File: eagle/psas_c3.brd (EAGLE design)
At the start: 100 x 80 mm, 61 parts, among them IC1 CP2102, U1 MIC5219 3.3V, Y1 32MHz

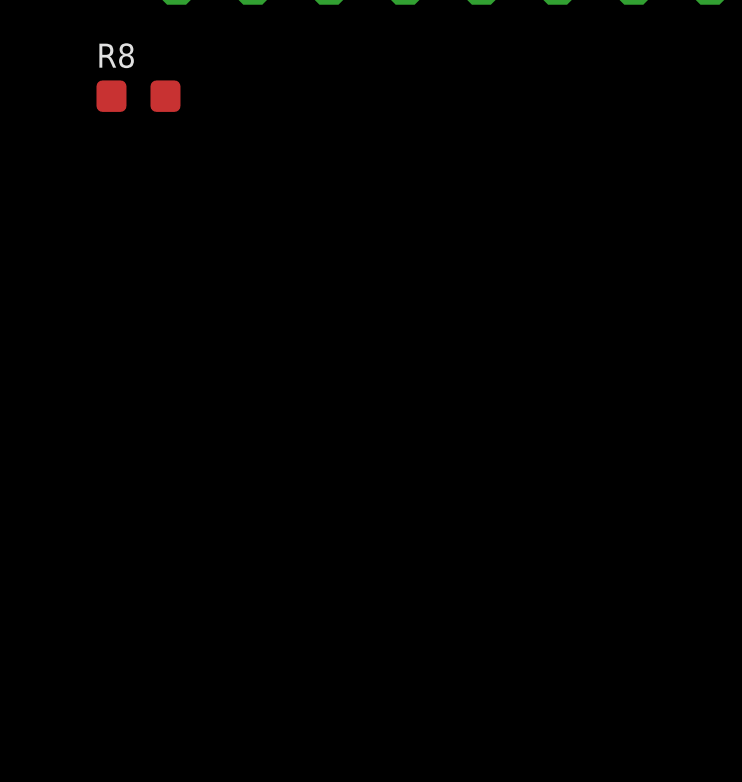
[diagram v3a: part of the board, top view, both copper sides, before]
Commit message: Added GPIO 2x9pins, 2x10 pins and SW Connector
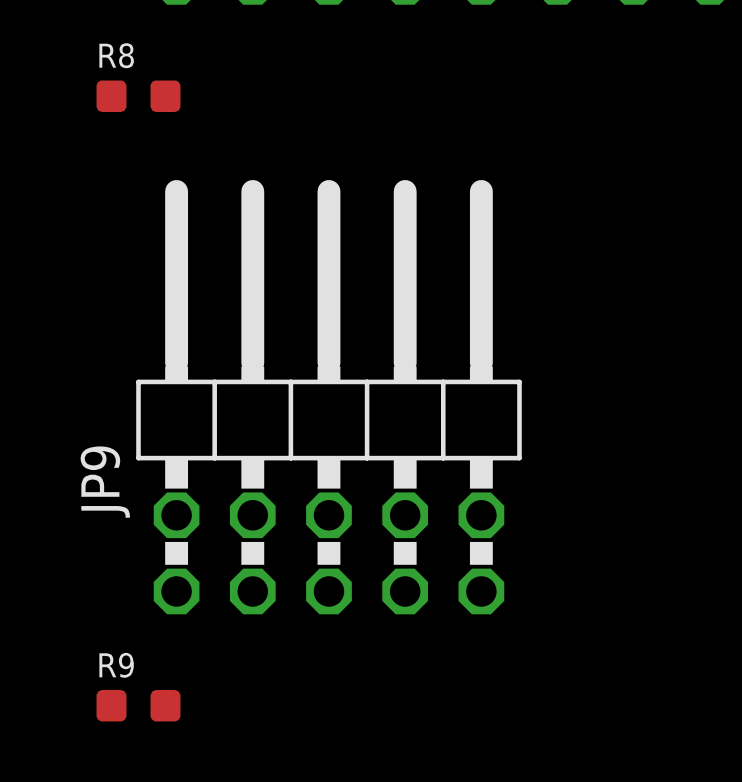
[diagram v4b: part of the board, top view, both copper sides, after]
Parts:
- added JP9: (no value), pinhead:2X05/90
- added R9: 10k, rcl_custom:.0603-A-NOSILK
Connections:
- new net PTA0: JP9.4, U$1.10
- new net PTA3: JP9.2, R9.1, U$1.11
- net 3.3V: now also R9.2
- net GND: now also JP9.3, JP9.5
- net PTA20: now also JP9.10
- net V+: now also JP9.1
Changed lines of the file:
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@@
 <element name="JP8" library="pinhead" package="2X10/90" value="" x="-63.5" y="-107.95"/>
 <element name="R8" library="rcl_custom" package=".0603-A-NOSILK" value="0" x="-76.2" y="-118.11"/>
+<element name="JP9" library="pinhead" package="2X05/90" value="" x="-69.85" y="-128.27"/>
+<element name="R9" library="rcl_custom" package=".0603-A-NOSILK" value="10k" x="-76.2" y="-138.43"/>
 </elements>
 <signals>
@@
 <contactref element="JP8" pad="15"/>
 <contactref element="JP8" pad="3"/>
+<contactref element="JP9" pad="5"/>
+<contactref element="JP9" pad="3"/>
+<wire x1="-69.85" y1="-134.62" x2="-72.39" y2="-134.62" width="0" layer="19" extent="1-1"/>
+<wire x1="-72.39" y1="-114.3" x2="-72.39" y2="-134.62" width="0" layer="19" extent="1-1"/>
 <wire x1="-57.15" y1="-114.3" x2="-72.39" y2="-114.3" width="0" layer="19" extent="1-1"/>
 <wire x1="-62.23" y1="-86.36" x2="-57.15" y2="-114.3" width="0" layer="19" extent="1-1"/>
@@
 <contactref element="R6" pad="2"/>
 <contactref element="JP5" pad="1"/>
+<contactref element="R9" pad="2"/>
+<wire x1="-66.51" y1="-73.66" x2="-75.3" y2="-138.43" width="0" layer="19" extent="1-1"/>
 <wire x1="-67.31" y1="-58.42" x2="-66.51" y2="-73.66" width="0" layer="19" extent="1-1"/>
 <wire x1="-56.68" y1="-44.45" x2="-67.31" y2="-58.42" width="0" layer="19" extent="1-1"/>
@@
 </signal>
 <signal name="VBUS">
-<contactref element="U2" pad="P$18"/>
-<contactref element="U2" pad="P$2"/>
-<contactref element="U2" pad="P$19"/>
-<contactref element="C1" pad="1"/>
-<contactref element="U2" pad="P$9"/>
-<contactref element="U2" pad="P$3"/>
 <contactref element="C17" pad="1"/>
 <contactref element="CF1" pad="1"/>
@@
 <contactref element="IC1" pad="7"/>
 <contactref element="LED1" pad="2"/>
+<contactref element="U2" pad="P$19"/>
+<contactref element="U2" pad="P$3"/>
+<contactref element="U2" pad="P$9"/>
+<contactref element="U2" pad="P$2"/>
+<contactref element="U2" pad="P$18"/>
+<contactref element="C1" pad="1"/>
 <contactref element="TP5" pad="1"/>
 <wire x1="-56.68" y1="-58.97" x2="-60.96" y2="-66.04" width="0" layer="19" extent="1-1"/>
@@
 <contactref element="JP6" pad="1"/>
 <contactref element="JP8" pad="1"/>
+<contactref element="JP9" pad="1"/>
+<wire x1="-74.93" y1="-114.3" x2="-74.93" y2="-134.62" width="0" layer="19" extent="1-1"/>
 <wire x1="-64.77" y1="-88.9" x2="-74.93" y2="-114.3" width="0" layer="19" extent="1-1"/>
 <wire x1="-39.1" y1="4.35" x2="-64.77" y2="-88.9" width="0" layer="19" extent="1-1"/>
@@
 <contactref element="S2" pad="A2"/>
 <contactref element="JP8" pad="10"/>
+<contactref element="JP9" pad="10"/>
+<wire x1="-64.77" y1="-111.76" x2="-64.77" y2="-132.08" width="0" layer="19" extent="1-1"/>
 <wire x1="-20.405" y1="24.11" x2="-64.77" y2="-111.76" width="0" layer="19" extent="1-1"/>
 <wire x1="-18.885" y1="28.23" x2="-20.405" y2="24.11" width="0" layer="19" extent="1-1"/>
@@
 <wire x1="-35.56" y1="29.21" x2="-26.38" y2="19.135" width="0" layer="19" extent="1-1"/>
 </signal>
+<signal name="PTA0">
+<contactref element="U$1" pad="10"/>
+<contactref element="JP9" pad="4"/>
+<wire x1="-27.855" y1="24.11" x2="-72.39" y2="-132.08" width="0" layer="19" extent="1-1"/>
+</signal>
+<signal name="PTA3">
+<contactref element="U$1" pad="11"/>
+<contactref element="JP9" pad="2"/>
+<contactref element="R9" pad="1"/>
+<wire x1="-74.93" y1="-132.08" x2="-77.1" y2="-138.43" width="0" layer="19" extent="1-1"/>
+<wire x1="-27.855" y1="24.61" x2="-74.93" y2="-132.08" width="0" layer="19" extent="1-1"/>
+</signal>
 </signals>

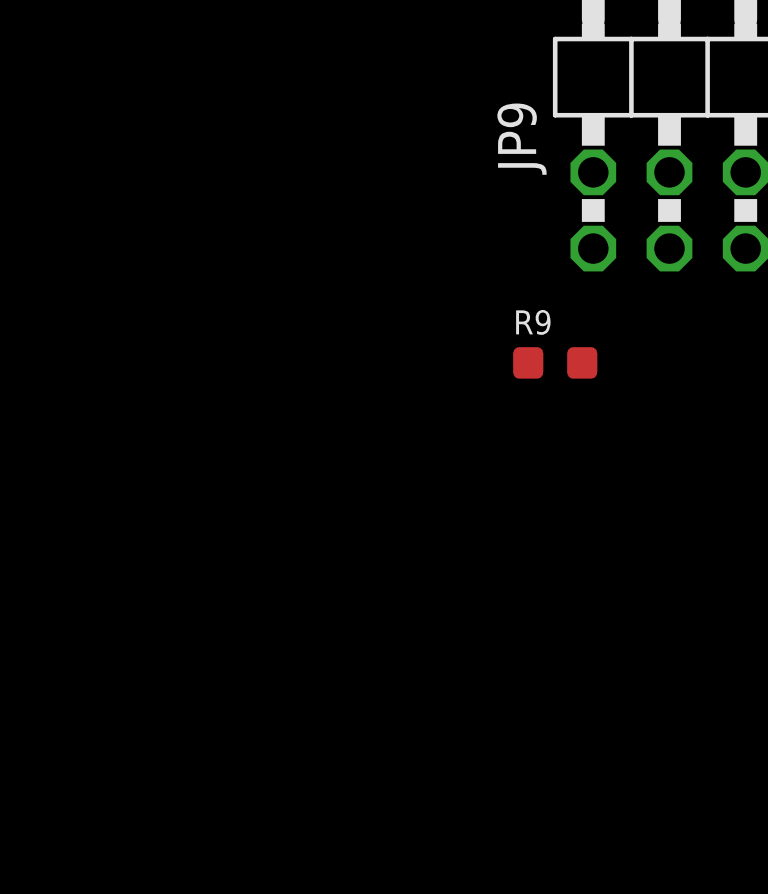
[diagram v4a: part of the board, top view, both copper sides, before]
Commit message: Added Software Development Connector and 32KHz crystal in schematics
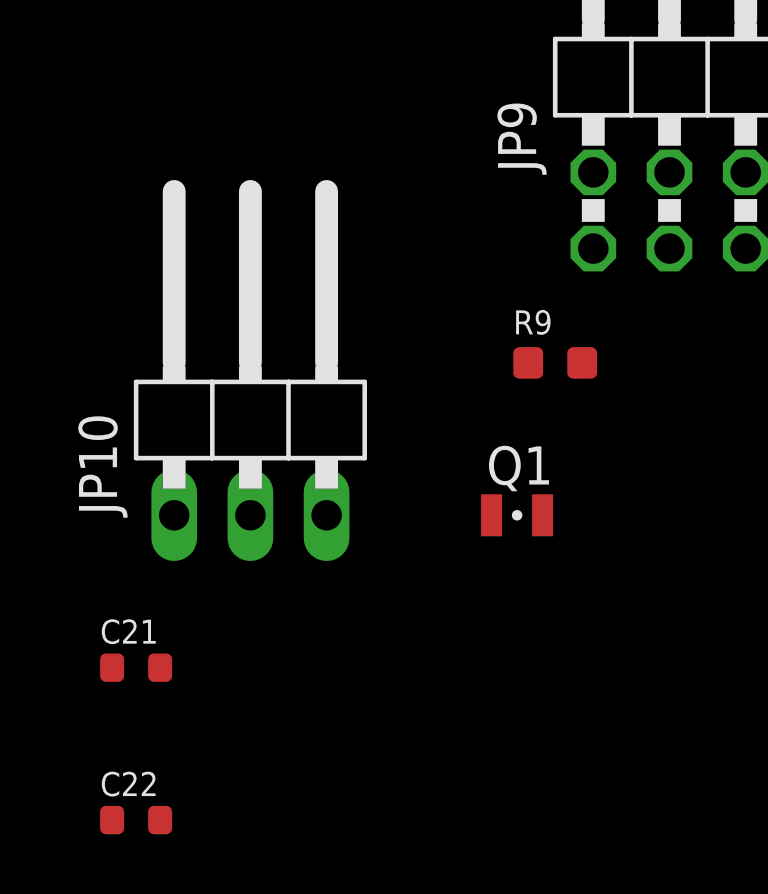
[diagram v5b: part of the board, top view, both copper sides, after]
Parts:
- added C21, C22: 12PF, rcl_custom:.0603-B-NOSILK
- added JP10: (no value), pinhead:1X03/90
- added Q1: FC-12M, crystal:FC-12M
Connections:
- new net N$13: C21.1, JP10.3, Q1.1
- net DIO5: now also JP10.1
- net GND: now also C21.2, C22.2
- net PTA18: now also JP10.2
- net PTA19: now also C22.1, Q1.2
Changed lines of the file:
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@@
 <element name="JP9" library="pinhead" package="2X05/90" value="" x="-69.85" y="-128.27"/>
 <element name="R9" library="rcl_custom" package=".0603-A-NOSILK" value="10k" x="-76.2" y="-138.43"/>
+<element name="Q1" library="crystal" package="FC-12M" value="FC-12M" x="-77.47" y="-143.51"/>
+<element name="JP10" library="pinhead" package="1X03/90" value="" x="-86.36" y="-139.7"/>
+<element name="C21" library="rcl_custom" package=".0603-B-NOSILK" value="12PF" x="-90.17" y="-148.59"/>
+<element name="C22" library="rcl_custom" package=".0603-B-NOSILK" value="12PF" x="-90.17" y="-153.67"/>
 </elements>
 <signals>
@@
 <contactref element="JP9" pad="5"/>
 <contactref element="JP9" pad="3"/>
+<contactref element="C21" pad="2"/>
+<contactref element="C22" pad="2"/>
+<wire x1="-89.37" y1="-148.59" x2="-89.37" y2="-153.67" width="0" layer="19" extent="1-1"/>
+<wire x1="-72.39" y1="-134.62" x2="-89.37" y2="-148.59" width="0" layer="19" extent="1-1"/>
 <wire x1="-69.85" y1="-134.62" x2="-72.39" y2="-134.62" width="0" layer="19" extent="1-1"/>
 <wire x1="-72.39" y1="-114.3" x2="-72.39" y2="-134.62" width="0" layer="19" extent="1-1"/>
@@
 <contactref element="U$1" pad="15"/>
 <contactref element="R8" pad="2"/>
+<contactref element="JP10" pad="2"/>
+<wire x1="-75.3" y1="-118.11" x2="-86.36" y2="-143.51" width="0" layer="19" extent="1-1"/>
 <wire x1="-38.1" y1="29.21" x2="-75.3" y2="-118.11" width="0" layer="19" extent="1-1"/>
 <wire x1="-27.38" y1="26.585" x2="-38.1" y2="29.21" width="0" layer="19" extent="1-1"/>
@@
 <contactref element="U$1" pad="16"/>
 <contactref element="R7" pad="1"/>
+<contactref element="Q1" pad="2"/>
+<contactref element="C22" pad="1"/>
+<wire x1="-76.62" y1="-143.51" x2="-90.97" y2="-153.67" width="0" layer="19" extent="1-1"/>
+<wire x1="-72.02" y1="-97.79" x2="-76.62" y2="-143.51" width="0" layer="19" extent="1-1"/>
 <wire x1="-26.88" y1="26.585" x2="-72.02" y2="-97.79" width="0" layer="19" extent="1-1"/>
 </signal>
@@
 <contactref element="JP2" pad="2"/>
 <contactref element="JP8" pad="16"/>
+<contactref element="JP10" pad="1"/>
+<wire x1="-57.15" y1="-111.76" x2="-88.9" y2="-143.51" width="0" layer="19" extent="1-1"/>
 <wire x1="-26.38" y1="19.135" x2="-57.15" y2="-111.76" width="0" layer="19" extent="1-1"/>
 <wire x1="-35.56" y1="29.21" x2="-26.38" y2="19.135" width="0" layer="19" extent="1-1"/>
@@
 <wire x1="-27.855" y1="24.61" x2="-74.93" y2="-132.08" width="0" layer="19" extent="1-1"/>
 </signal>
+<signal name="N$13">
+<contactref element="C21" pad="1"/>
+<contactref element="Q1" pad="1"/>
+<contactref element="JP10" pad="3"/>
+<wire x1="-83.82" y1="-143.51" x2="-90.97" y2="-148.59" width="0" layer="19" extent="1-1"/>
+<wire x1="-78.32" y1="-143.51" x2="-83.82" y2="-143.51" width="0" layer="19" extent="1-1"/>
+</signal>
 </signals>

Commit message: finished preliminary schematic layout, did a lot of reorganizing and cleaning up, added pin headers for i2c spi uart etc, passed erc with no errors but lots of warnings
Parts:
- removed C22: 12PF, rcl_custom:.0603-B-NOSILK
- removed Q1: FC-12M, crystal:FC-12M
- removed R6: (no value), rcl_custom:.0603-B-NOSILK
- removed R7, R8: 0, rcl_custom:.0603-A-NOSILK
- removed R9: 10k, rcl_custom:.0603-A-NOSILK
- removed TP6, TP7: (no value), psas_c3:1X01_ROUND
- added C23, C25: 100nF, Vibrogait_prototype:.0603-B-NOSILK
- added C24: 4.7uF, rcl_custom:.0603-B-NOSILK
- added D1, D2, D3: (no value), Vibrogait_prototype:SOD-123
- added JP11: (no value), SparkFun-v5:1X04
- added JP12, JP17: (no value), SparkFun-v5:1X02
- added JP13, JP14: M01PTH, SparkFun-v5:1X01
- added JP15: (no value), SparkFun-v5:1X05
- added JP16, JP18, JP19, JP20: (no value), SparkFun-v5:1X03
- added JP21: (no value), SparkFun-v5:1X06
- added JTAG1: (no value), microbuilder:CORTEXM3_SWD10_MOLEX
- C18: value 0.1uF -> 100nF; device rcl_custom:.0603-B-NOSILK -> Vibrogait_prototype:.0603-B-NOSILK
- C21: value 12PF -> 1nF
- JP10: device pinhead:1X03/90 -> SparkFun-v5:1X03
- JP3: device pinhead:1X02 -> SparkFun-v5:1X02
- JP4: device pinhead:1X02 -> SparkFun-v5:1X03
- JP5: value M05X2PTH -> (none); device SparkFun-v5:AVR_ICSP -> SparkFun-v5:1X03
- JP6: device pinhead:2X09/90 -> SparkFun-v5:1X03
- JP8: device pinhead:2X10/90 -> SparkFun-v5:1X02
- JP9: device pinhead:2X05/90 -> SparkFun-v5:1X03
- R1: value (none) -> 1k
- RP2: value 4.7 -> 4.7k
- moved R1 373.7 mm to (-90.2, -317.5)
- moved S2 358.7 mm to (-86.4, -322.6)
- moved JP3 209.0 mm to (-88.9, -217.2)
- moved JP4 207.7 mm to (-88.9, -222.2)
- moved C21 179.1 mm to (-90.2, -327.7)
- moved JP5 165.4 mm to (-88.9, -227.3)
- moved C18 153.7 mm to (-90.2, -184.2)
- moved JP6 153.7 mm to (-88.9, -232.4)
- moved JP7 145.1 mm to (-88.9, -237.5)
- moved JP8 137.0 mm to (-88.9, -242.6)
- moved JP9 120.9 mm to (-88.9, -247.7)
- moved JP10 113.1 mm to (-88.9, -252.7)
- renumbered RP4 to R14
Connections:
- removed net DIO2: JP6.17, TP6.1, U$1.51
- removed net DIO3: JP6.6, TP7.1, U$1.52
- removed net DIO4: JP7.2, U$1.53
- removed net DIO5: JP10.1, JP2.2, JP8.16, U$1.54
- removed net N$15: JP6.2, R8.1
- removed net N$23: JP3.2, U$1.1
- removed net N$24: JP5.6
- removed net N$25: CF1.3, IC1.4
- removed net N$28: IC1.25, U$1.14
- removed net N$29: IC1.26, U$1.13
- removed net N$31: CF1.2, IC1.5
- removed net N$36: JP5.7
- removed net N$37: JP5.9
- removed net N$40: JP6.3, R7.2
- removed net PTA20: JP8.10, JP9.10, R1.1, S2.A2, U$1.33
- removed net VBAT1: U$1.43
- removed net VBAT2: U$1.35
- removed net VDDA: U$1.56
- removed net VSSA: U$1.3
- new net D+: CF1.3, D1.CATHODE, IC1.4
- new net D-: CF1.2, D2.CATHODE, IC1.5
- new net DIO5/CLKOUT: JP2.2, JP21.6, U$1.54
- new net N$14: C25.1, U$1.44
- new net PTA1: IC1.25, JP3.2, U$1.14
- new net PTA2: IC1.26, JP4.3, U$1.13
- new net PTA20/!RESET: C21.1, JTAG1.10, R1.1, S2.A2, U$1.33
- new net PTC5: JP12.2, U$1.59
- new net PTC6: JP10.3, JP11.3, U$1.60
- new net PTC7: JP11.4, U$1.57
- new net PTD0: JP9.2, U$1.58
- new net PTE3: JP15.2, JP16.3, U$1.50
- net 3.3V: now also C18.1, JTAG1.1, U$1.1, U$1.35, U$1.43, U$1.56; no longer JP3.1, JP5.1, R6.2, R9.2
- net GND: now also C23.2, C24.2, C25.2, D1.ANODE, D2.ANODE, D3.ANODE, JTAG1.3, JTAG1.5, JTAG1.9, U$1.2, U$1.3; no longer C22.2, JP4.1, JP5.3, JP5.5, JP6.18, JP6.4, JP8.15, JP8.3, JP9.3, JP9.5
- net N$13: now also JP21.5, U$1.53; no longer C21.1, JP10.3, Q1.1
- net N$22: now also C23.1, U$1.45; no longer JP4.2, U$1.2
- net N$27: now also C24.1
- net N$30: now also IC1.1, IC1.2, IC1.27, IC1.28
- net N$5: now also JP21.3, U$1.51; no longer JP5.2, R6.1
- net N$7: now also JP21.4, U$1.52; no longer JP5.4
- net PTA0: now also JTAG1.4; no longer JP9.4
- net PTA18: now also JP5.3; no longer JP10.2, R8.2
- net PTA19: now also JP6.3; no longer C22.1, Q1.2, R7.1
- net PTA3: now also JP20.3, JTAG1.2; no longer JP9.2, R9.1
- net PTA4: now also JP19.3; no longer JP8.17
- net PTB0: now also JP18.3; no longer JP8.9
- net PTB1: now also JP17.2, U$1.48; no longer JP6.8
- net PTB17: now also JP15.1, JP4.1; no longer JP8.14
- net PTB2: now also JP18.2; no longer JP8.12
- net PTC1: now also JP20.1; no longer JP8.13
- net PTC2: now also JP19.1; no longer JP8.11
- net PTC3: now also JP5.2; no longer JP6.9
- net PTC4: now also JP6.2, JP9.3; no longer JP6.13
- net PTD4: now also JP13.1, JP7.2, U$1.27; no longer JP6.16, JP7.1
- net PTD5: now also JP8.2; no longer JP8.18
- net PTD6: now also JP15.5, JP3.1; no longer JP8.19
- net PTD7: now also JP11.1, JP15.4, JP4.2; no longer JP8.20
- net PTE0: now also JP16.2, JP19.2, JP6.1; no longer JP6.12
- net PTE1: now also JP15.3, JP16.1, JP20.2, JP5.1; no longer JP6.14
- net PTE16: now also JP8.1, JP9.1; no longer JP6.7
- net PTE17: now also JP12.1, JP7.1; no longer JP6.15
- net PTE18: now also JP10.2, JP17.1; no longer JP6.10
- net PTE19: now also JP10.1, JP11.2, JP18.1; no longer JP6.11
- net PTE2: now also JP14.1; no longer JP6.5
- net V+: no longer JP6.1, JP8.1, JP9.1
- net VBUS: no longer C18.1

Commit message: First few changes submitted
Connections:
- removed net PTA20/!RESET: C21.1, JTAG1.10, R1.1, S2.A2, U$1.33
- new net N$15: C21.1, R1.1, S2.A2
- new net N$24: C1.1
- new net N$26: LED1.2, U2.P$18, U2.P$19, U2.P$2, U2.P$3, U2.P$9
- new net RESET: JTAG1.10, U$1.33
- net PTA1: no longer IC1.25
- net PTA18: no longer JP2.1
- net PTA2: no longer IC1.26
- net VBUS: no longer C1.1, LED1.2, U2.P$18, U2.P$19, U2.P$2, U2.P$3, U2.P$9
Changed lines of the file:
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@@
 <?xml version="1.0" encoding="utf-8"?>
 <!DOCTYPE eagle SYSTEM "eagle.dtd">
-<eagle version="7.3.0">
+<eagle version="7.4.0">
 <drawing>
 <settings>
@@
 <contactref element="CF1" pad="1"/>
 <contactref element="IC1" pad="7"/>
-<contactref element="LED1" pad="2"/>
-<contactref element="U2" pad="P$19"/>
-<contactref element="U2" pad="P$3"/>
-<contactref element="U2" pad="P$9"/>
-<contactref element="U2" pad="P$2"/>
-<contactref element="U2" pad="P$18"/>
-<contactref element="C1" pad="1"/>
 <contactref element="TP5" pad="1"/>
 <contactref element="IC1" pad="8"/>
-<wire x1="-56.68" y1="-58.97" x2="-60.96" y2="-66.04" width="0" layer="19" extent="1-1"/>
-<wire x1="-56.68" y1="-29.21" x2="-56.68" y2="-58.97" width="0" layer="19" extent="1-1"/>
+<wire x1="-56.68" y1="-29.21" x2="-60.96" y2="-66.04" width="0" layer="19" extent="1-1"/>
 <wire x1="-56.11" y1="-22.62" x2="-56.68" y2="-29.21" width="0" layer="19" extent="1-1"/>
 <wire x1="-56.91" y1="-21.82" x2="-56.11" y2="-22.62" width="0" layer="19" extent="1-1"/>
 <wire x1="-35.59" y1="22.995" x2="-56.91" y2="-21.82" width="0" layer="19" extent="1-1"/>
-<wire x1="-17.205" y1="30.48" x2="-35.59" y2="22.995" width="0" layer="19" extent="1-1"/>
-<wire x1="-17.205" y1="30.98" x2="-17.205" y2="30.48" width="0" layer="19" extent="1-1"/>
-<wire x1="-15.74" y1="32.445" x2="-17.205" y2="30.98" width="0" layer="19" extent="1-1"/>
-<wire x1="-15.24" y1="32.445" x2="-15.74" y2="32.445" width="0" layer="19" extent="1-1"/>
-<wire x1="-14.74" y1="28.515" x2="-17.205" y2="30.48" width="0" layer="19" extent="1-1"/>
-<wire x1="-30.01" y1="46.99" x2="-15.74" y2="32.445" width="0" layer="19" extent="1-1"/>
 </signal>
 <signal name="V+">
@@
 <signal name="PTA1">
 <contactref element="U$1" pad="14"/>
-<contactref element="IC1" pad="25"/>
 <contactref element="JP3" pad="2"/>
-<wire x1="-27.855" y1="26.11" x2="-54.61" y2="-18.02" width="0" layer="19" extent="1-1"/>
-<wire x1="-86.36" y1="-217.17" x2="-54.61" y2="-18.02" width="0" layer="19" extent="1-1"/>
+<wire x1="-27.855" y1="26.11" x2="-86.36" y2="-217.17" width="0" layer="19" extent="1-1"/>
 </signal>
 <signal name="PTA2">
 <contactref element="U$1" pad="13"/>
-<contactref element="IC1" pad="26"/>
 <contactref element="JP4" pad="3"/>
-<wire x1="-27.855" y1="25.61" x2="-55.11" y2="-18.02" width="0" layer="19" extent="1-1"/>
-<wire x1="-83.82" y1="-222.25" x2="-55.11" y2="-18.02" width="0" layer="19" extent="1-1"/>
+<wire x1="-27.855" y1="25.61" x2="-83.82" y2="-222.25" width="0" layer="19" extent="1-1"/>
 </signal>
 <signal name="N$30">
@@
 <contactref element="U$1" pad="15"/>
 <contactref element="JP5" pad="3"/>
-<contactref element="JP2" pad="1"/>
 <wire x1="-27.38" y1="26.585" x2="-83.82" y2="-227.33" width="0" layer="19" extent="1-1"/>
-<wire x1="-38.1" y1="29.21" x2="-27.38" y2="26.585" width="0" layer="19" extent="1-1"/>
 </signal>
 <signal name="N$22">
@@
 <contactref element="C25" pad="1"/>
 <wire x1="-21.38" y1="19.135" x2="-90.97" y2="-194.31" width="0" layer="19" extent="1-1"/>
-</signal>
-<signal name="PTA20/!RESET">
-<contactref element="U$1" pad="33"/>
-<contactref element="JTAG1" pad="10"/>
-<contactref element="R1" pad="1"/>
-<contactref element="S2" pad="A2"/>
-<contactref element="C21" pad="1"/>
-<wire x1="-82.385" y1="-324.83" x2="-90.97" y2="-327.66" width="0" layer="19" extent="1-1"/>
-<wire x1="-90.97" y1="-317.5" x2="-90.97" y2="-327.66" width="0" layer="19" extent="1-1"/>
-<wire x1="-74.93" y1="-207.01" x2="-90.97" y2="-317.5" width="0" layer="19" extent="1-1"/>
-<wire x1="-20.405" y1="24.11" x2="-74.93" y2="-207.01" width="0" layer="19" extent="1-1"/>
 </signal>
 <signal name="PTA3">
@@
 <wire x1="-25.88" y1="19.135" x2="-78.74" y2="-313.69" width="0" layer="19" extent="1-1"/>
 </signal>
+<signal name="N$15">
+<contactref element="R1" pad="1"/>
+<contactref element="S2" pad="A2"/>
+<contactref element="C21" pad="1"/>
+<wire x1="-82.385" y1="-324.83" x2="-90.97" y2="-327.66" width="0" layer="19" extent="1-1"/>
+<wire x1="-90.97" y1="-317.5" x2="-90.97" y2="-327.66" width="0" layer="19" extent="1-1"/>
+</signal>
+<signal name="RESET">
+<contactref element="U$1" pad="33"/>
+<contactref element="JTAG1" pad="10"/>
+<wire x1="-20.405" y1="24.11" x2="-74.93" y2="-207.01" width="0" layer="19" extent="1-1"/>
+</signal>
+<signal name="N$26">
+<contactref element="U2" pad="P$2"/>
+<contactref element="U2" pad="P$9"/>
+<contactref element="U2" pad="P$3"/>
+<contactref element="U2" pad="P$19"/>
+<contactref element="LED1" pad="2"/>
+<contactref element="U2" pad="P$18"/>
+<wire x1="-14.74" y1="28.515" x2="-56.68" y2="-58.97" width="0" layer="19" extent="1-1"/>
+<wire x1="-17.205" y1="30.48" x2="-14.74" y2="28.515" width="0" layer="19" extent="1-1"/>
+<wire x1="-17.205" y1="30.98" x2="-17.205" y2="30.48" width="0" layer="19" extent="1-1"/>
+<wire x1="-15.74" y1="32.445" x2="-17.205" y2="30.98" width="0" layer="19" extent="1-1"/>
+<wire x1="-15.24" y1="32.445" x2="-15.74" y2="32.445" width="0" layer="19" extent="1-1"/>
+</signal>
+<signal name="N$24">
+<contactref element="C1" pad="1"/>
+</signal>
 </signals>
